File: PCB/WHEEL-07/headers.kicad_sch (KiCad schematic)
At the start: 3 parts

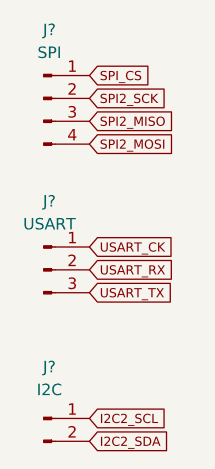
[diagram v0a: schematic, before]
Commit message: Configured library loader for this project
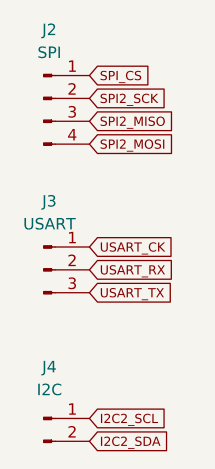
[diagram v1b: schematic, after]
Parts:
- gave numbers to parts that had none: 3
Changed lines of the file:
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@@
   (symbol (lib_id "Connector:Conn_01x04_Male") (at 36.83 31.75 0) (unit 1)
     (in_bom yes) (on_board yes) (fields_autoplaced)
-    (property "Reference" "J?" (id 0) (at 37.465 24.13 0))
+    (property "Reference" "J2" (id 0) (at 37.465 24.13 0))
     (property "Value" "SPI" (id 1) (at 37.465 26.67 0))
     (property "Footprint" "" (id 2) (at 36.83 31.75 0)
@@
   (symbol (lib_id "Connector:Conn_01x02_Male") (at 36.83 67.31 0) (unit 1)
     (in_bom yes) (on_board yes) (fields_autoplaced)
-    (property "Reference" "J?" (id 0) (at 37.465 61.595 0))
+    (property "Reference" "J4" (id 0) (at 37.465 61.595 0))
     (property "Value" "I2C" (id 1) (at 37.465 64.135 0))
     (property "Footprint" "" (id 2) (at 36.83 67.31 0)
@@
   (symbol (lib_id "Connector:Conn_01x03_Male") (at 36.83 50.8 0) (unit 1)
     (in_bom yes) (on_board yes) (fields_autoplaced)
-    (property "Reference" "J?" (id 0) (at 37.465 43.18 0))
+    (property "Reference" "J3" (id 0) (at 37.465 43.18 0))
     (property "Value" "USART" (id 1) (at 37.465 45.72 0))
     (property "Footprint" "" (id 2) (at 36.83 50.8 0)

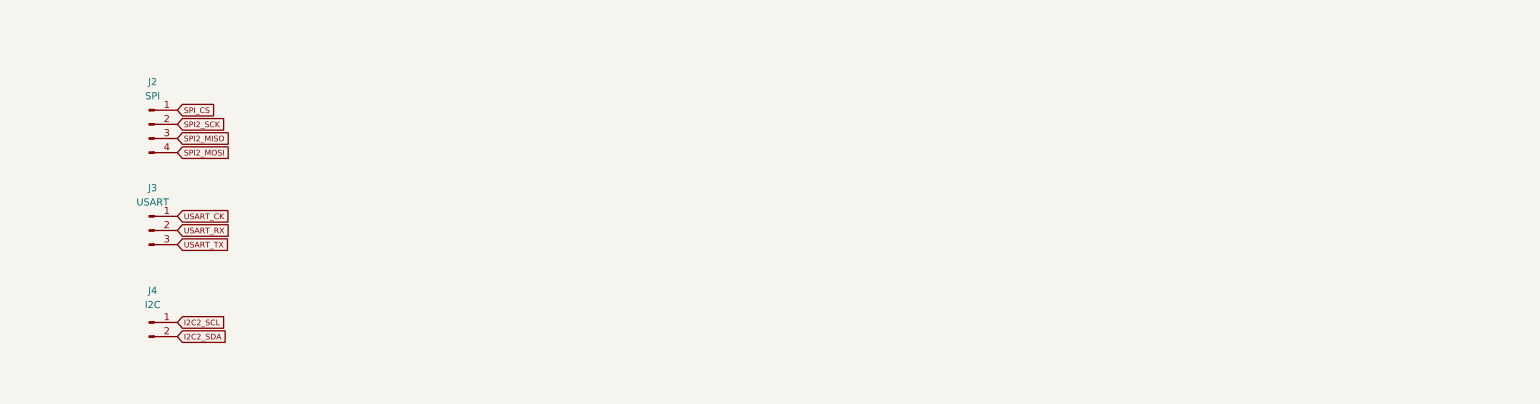
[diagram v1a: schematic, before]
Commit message: Modified layout
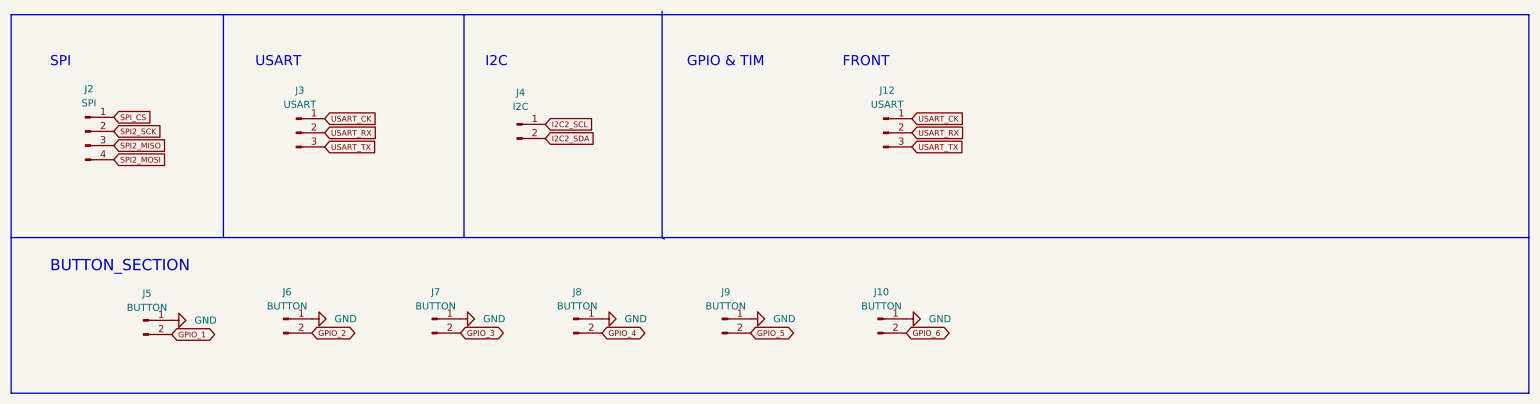
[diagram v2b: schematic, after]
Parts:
- added J10, J5, J6, J7, J8, J9: BUTTON, Connector_Molex:Molex_PicoBlade_53047-0210_1x02_P1.25mm_Vertical, symbol Connector:Conn_01x02_Male
- added J12: USART, Connector_Molex:Molex_PicoBlade_53047-0310_1x03_P1.25mm_Vertical, symbol Connector:Conn_01x03_Male
- J2, J3: footprint (none) -> Connector_Molex:Molex_PicoBlade_53047-0310_1x03_P1.25mm_Vertical
- J4: footprint (none) -> Connector_Molex:Molex_PicoBlade_53047-0210_1x02_P1.25mm_Vertical
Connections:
- net USART_CK: now also J12.1 (Pin_1)
- net USART_RX: now also J12.2 (Pin_2)
- net USART_TX: now also J12.3 (Pin_3)
- new net GND: J10.1 (Pin_1), J5.1 (Pin_1), J6.1 (Pin_1), J7.1 (Pin_1), J8.1 (Pin_1), J9.1 (Pin_1)
- new net GPIO_1: J5.2 (Pin_2)
- new net GPIO_2: J6.2 (Pin_2)
- new net GPIO_3: J7.2 (Pin_2)
- new net GPIO_4: J8.2 (Pin_2)
- new net GPIO_5: J9.2 (Pin_2)
- new net GPIO_6: J10.2 (Pin_2)
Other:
- note added: "BUTTON_SECTION"
- note added: "FRONT"
- note added: "GPIO & TIM"
- note added: "I2C"
- note added: "SPI"
- note added: "USART"
- moved on the sheet: J2, J3, J4

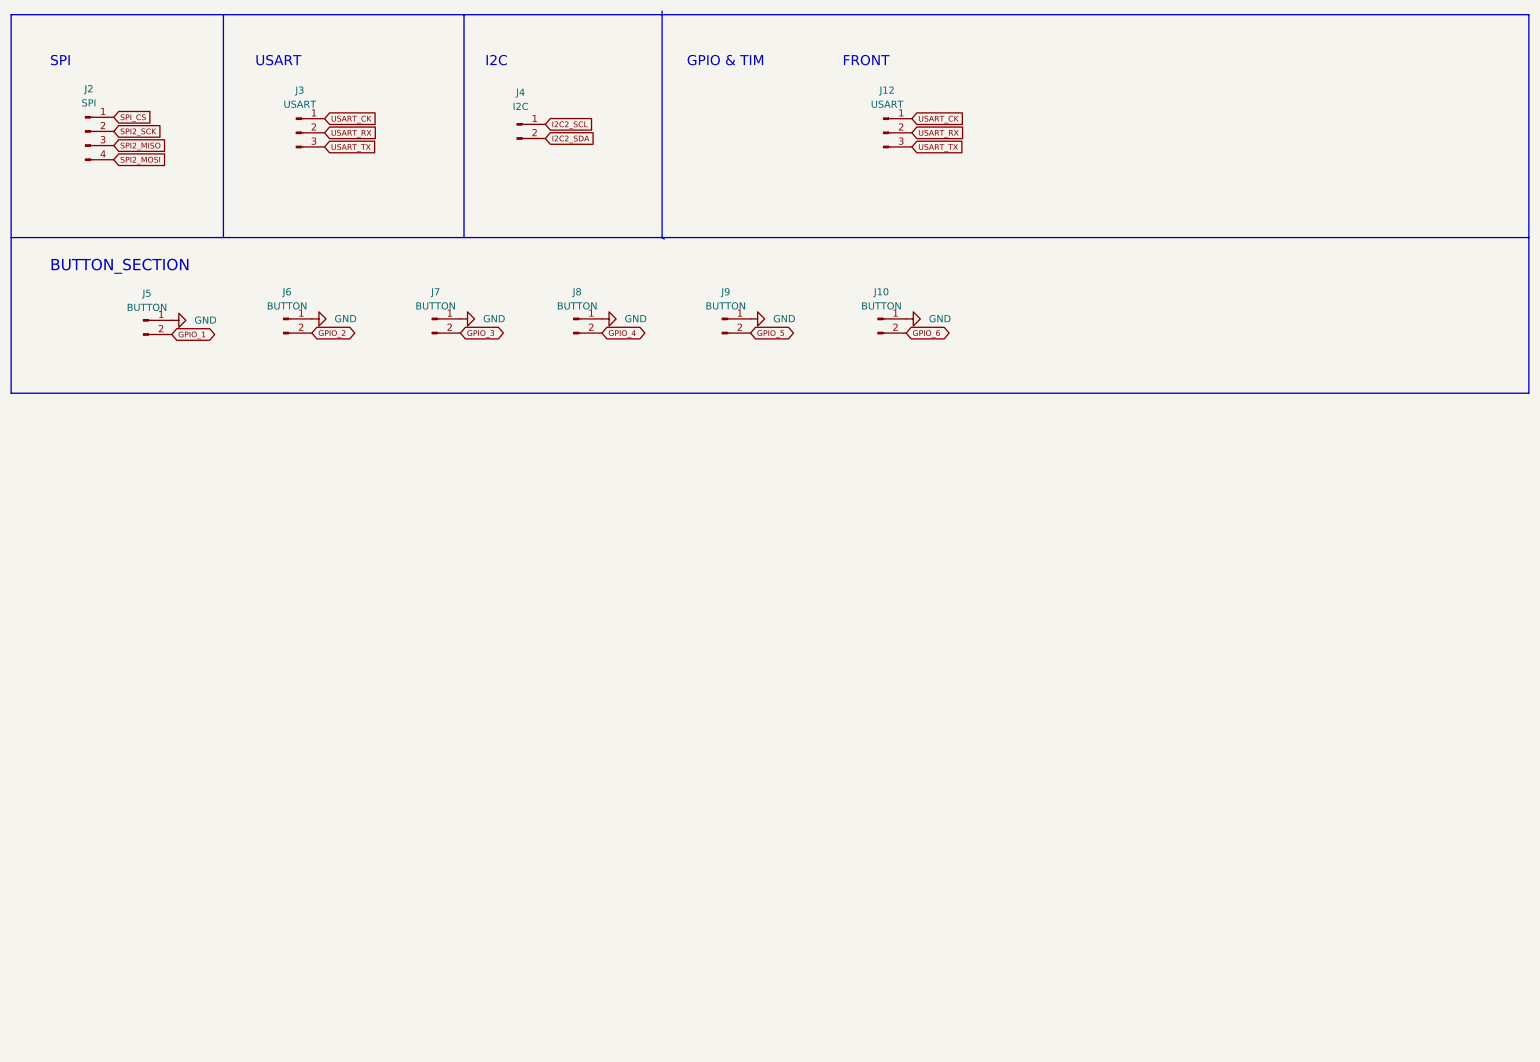
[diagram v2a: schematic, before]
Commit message: Added paddles hardware debouncing to PCB
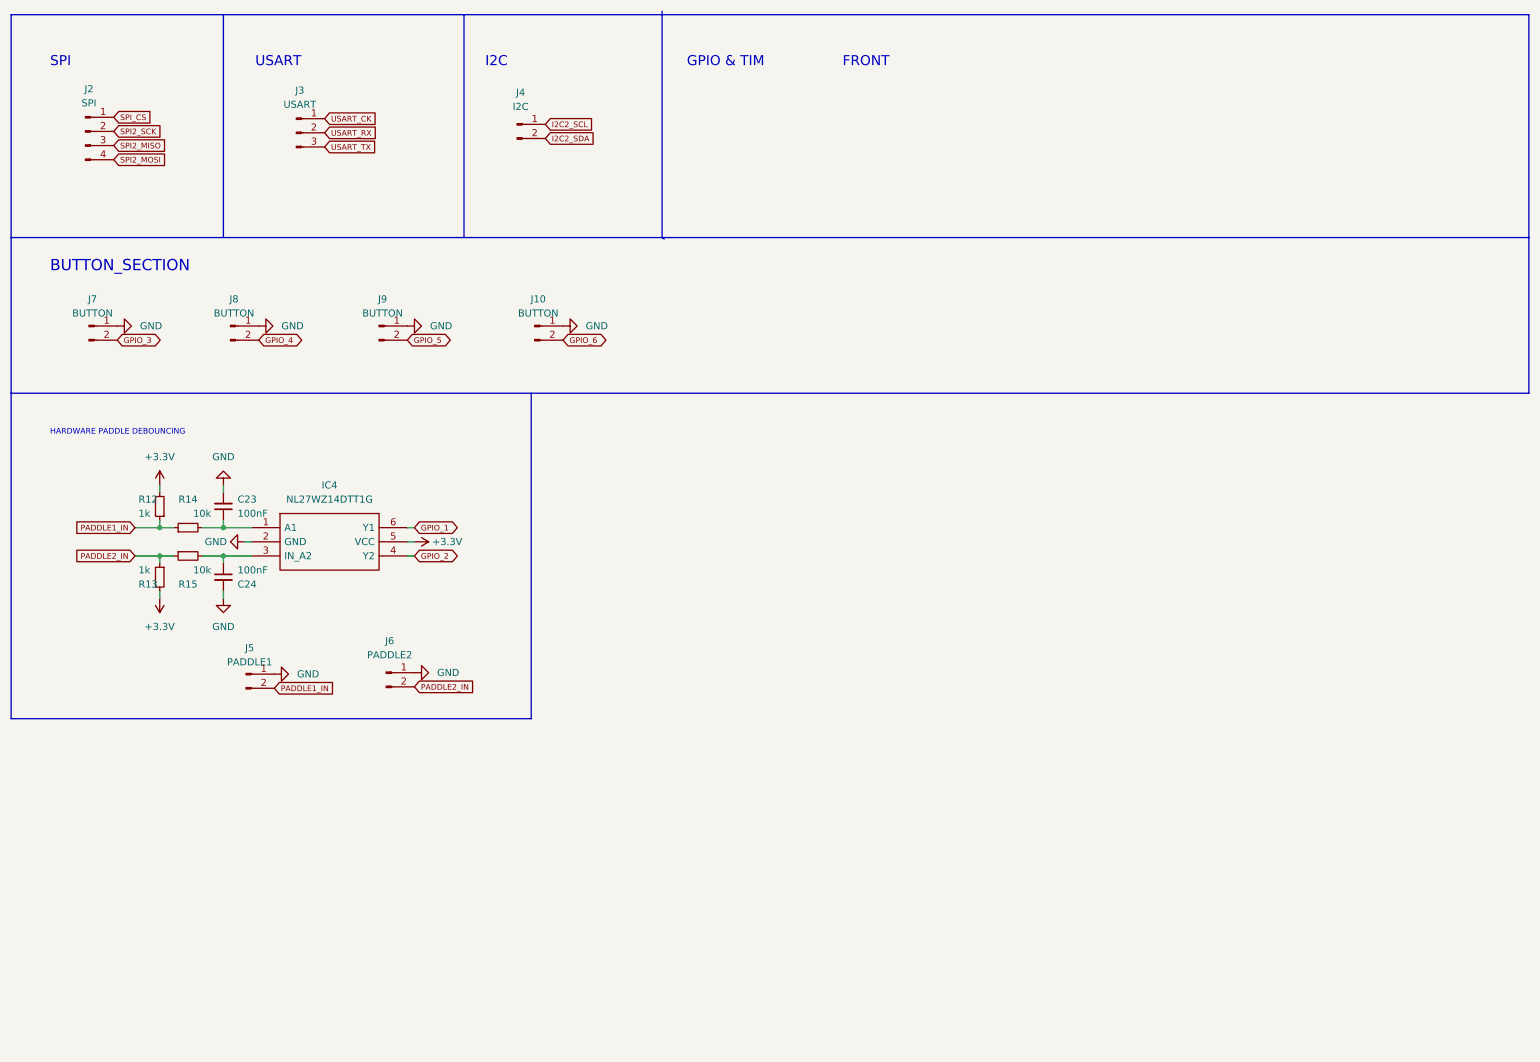
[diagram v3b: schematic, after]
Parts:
- removed J12: USART, Connector_Molex:Molex_PicoBlade_53047-0310_1x03_P1.25mm_Vertical, symbol Connector:Conn_01x03_Male
- added C23, C24: 100nF, symbol Device:C_Small
- added IC4: NL27WZ14DTT1G, SOT95P275X110-6N, symbol WHEEL_07_LIBRARY_LOADER:NL27WZ14DTT1G
- added R12, R13: 1k, symbol Device:R_Small
- added R14, R15: 10k, symbol Device:R_Small
- J5: value BUTTON -> PADDLE1
- J6: value BUTTON -> PADDLE2
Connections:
- net GND: now also C23.2, C24.2, IC4.2 (GND)
- net GPIO_1: now also IC4.6 (Y1); no longer J5.2 (Pin_2)
- net GPIO_2: now also IC4.4 (Y2); no longer J6.2 (Pin_2)
- new net: C23.1, IC4.1 (A1), R14.2
- new net: C24.1, IC4.3 (IN_A2), R15.2
- new net +3.3V: IC4.5 (VCC), R12.2, R13.2
- new net PADDLE1_IN: J5.2 (Pin_2), R12.1, R14.1
- new net PADDLE2_IN: J6.2 (Pin_2), R13.1, R15.1
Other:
- note added: "HARDWARE PADDLE DEBOUNCING"
- moved on the sheet: J10, J5, J6, J7, J8, J9

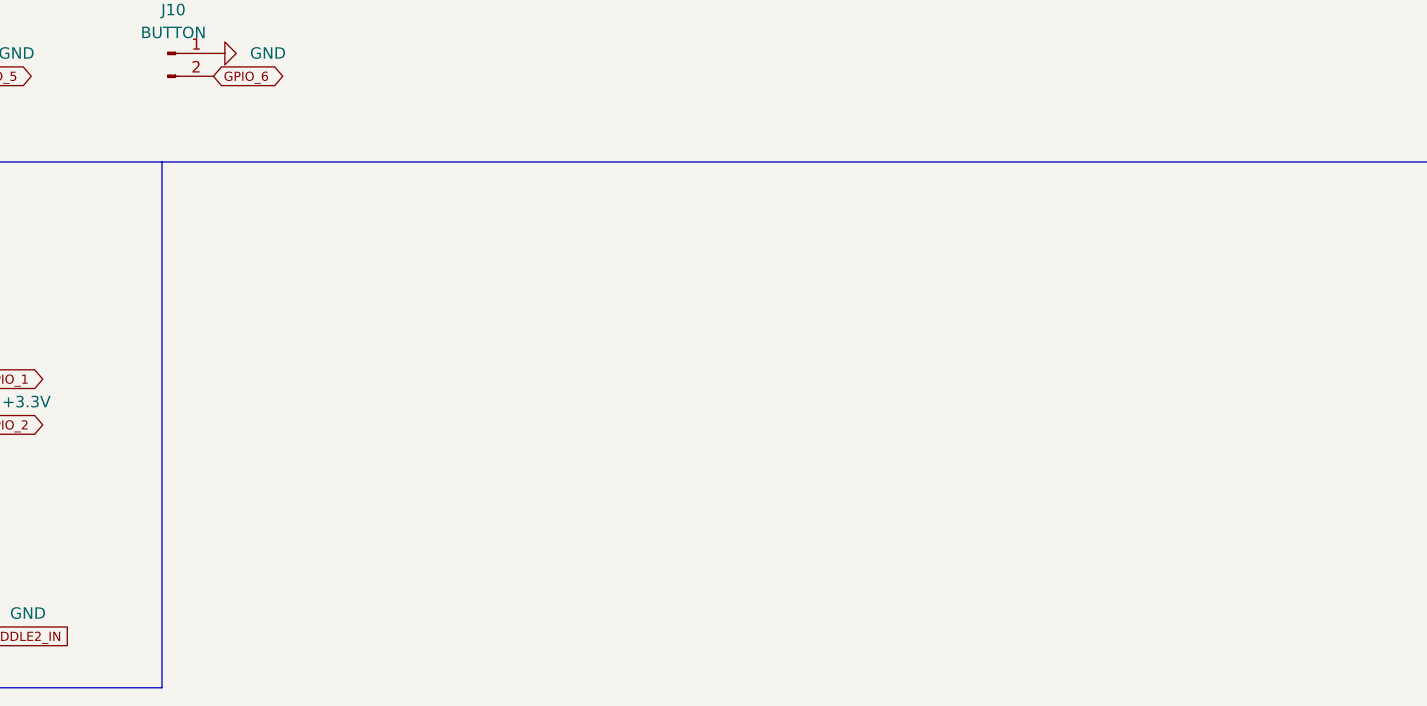
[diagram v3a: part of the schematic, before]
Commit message: Added rotaries
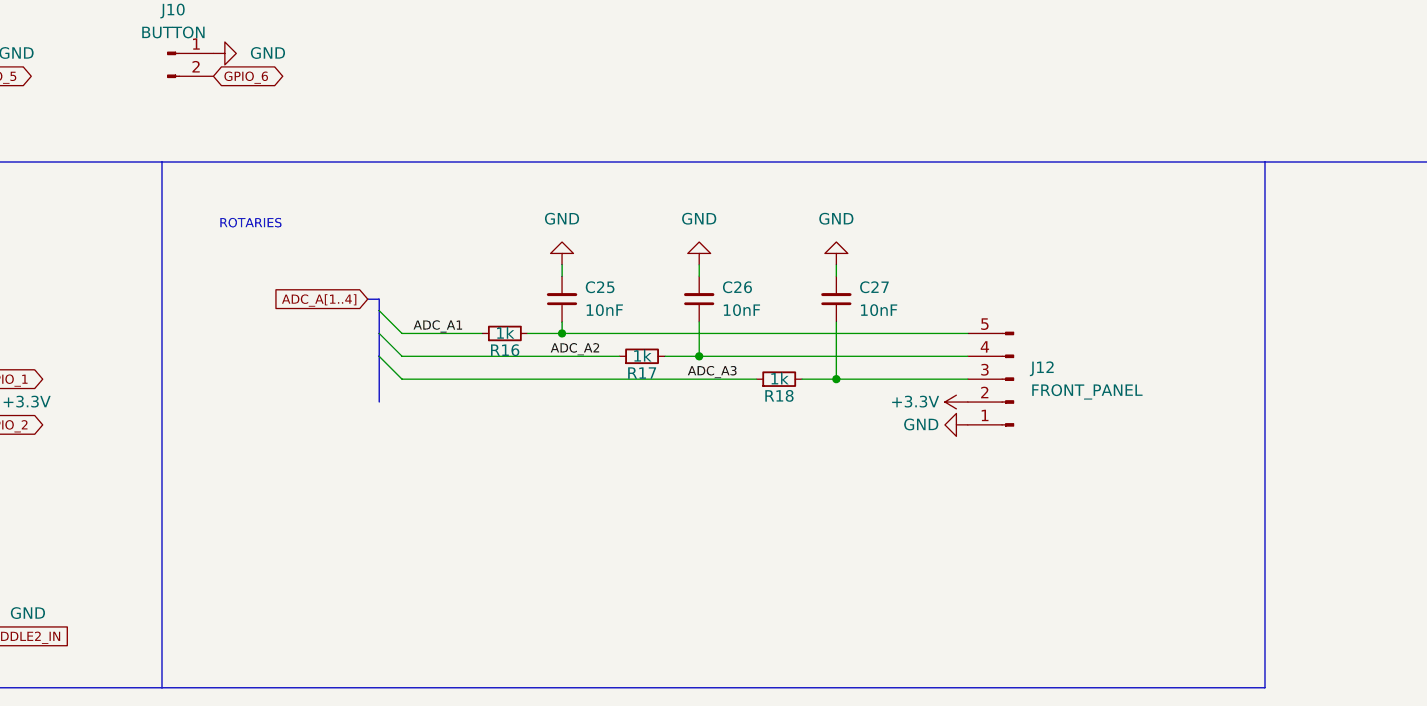
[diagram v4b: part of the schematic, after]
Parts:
- added C25, C26, C27: 10nF, symbol Device:C_Small
- added J12: FRONT_PANEL, symbol Connector:Conn_01x05_Male
- added R16, R17, R18: 1k, Resistor_SMD:R_0402_1005Metric, symbol Device:R_Small
- IC4: footprint SOT95P275X110-6N -> WHEEL_07_LIBRARY_LOADER:SOT95P275X110-6N
- R12, R13, R14, R15: footprint (none) -> Resistor_SMD:R_0402_1005Metric
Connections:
- net +3.3V: now also J12.2 (Pin_2)
- net GND: now also C25.2, C26.2, C27.2, J12.1 (Pin_1)
- new net: C25.1, J12.5 (Pin_5), R16.2
- new net: C27.1, J12.3 (Pin_3), R18.2
- new net: C26.1, J12.4 (Pin_4), R17.2
- new net ADC_A1: R16.1
- new net ADC_A2: R17.1
- new net ADC_A3: R18.1
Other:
- note added: "ROTARIES"
